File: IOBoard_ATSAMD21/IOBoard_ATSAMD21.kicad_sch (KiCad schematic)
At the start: 36 parts, among them J1 Conn_PIC_ICSP_ICD, J2 Conn_01x04_Male, SW1 EG_1218, SW2 EG_1218, SW3 EG_1218, SW4 EG_1218, U1 ATSAMD21G18A-A, U2 AP2112K-3.3

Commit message: IOBoard V2 + documentation
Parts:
- ENC0, ENC1, ENC2, ENC3: footprint Rotary_Encoder:RotaryEncoder_Bourns_Vertical_PEC12R-3xxxF-Sxxxx -> custom_lib:PEC12R-3217F-S0024-ND
- H1, H2, H3, H4: footprint MountingHole:MountingHole_2.2mm_M2_Pad -> MountingHole:MountingHole_3.2mm_M3_ISO7380_Pad
- SW1, SW2, SW3, SW4: footprint Custom:EG_1218 -> custom_lib:EG_1218
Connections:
- net GND: now also R1.1, R2.1, R3.1, R4.1; no longer D1.1 (K), D2.1 (K), D3.1 (K), D4.1 (K)
- net LED0: now also D1.2 (A); no longer R1.2
- net LED1: now also D2.2 (A); no longer R2.2
- net LED2: now also D3.2 (A); no longer R3.2
- net LED3: now also D4.2 (A); no longer R4.2
- net SCL: now also J2.3 (Pin_3); no longer J2.4 (Pin_4)
- net SDA: now also J2.4 (Pin_4); no longer J2.3 (Pin_3)
- new net: D2.1 (K), R2.2
- new net: D1.1 (K), R1.2
- new net: D4.1 (K), R4.2
- new net: D3.1 (K), R3.2
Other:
- moved on the sheet: R1, R2, R3, R4

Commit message: cleaned up'
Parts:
- added S? (x3): EG1218, digikey-footprints:Switch_Slide_11.6x4mm_EG1218, symbol dk_Slide-Switches:EG1218
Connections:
- new net Line In 1: S?.3
- new net Line In 2: S?.1
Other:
- note added: "CV config"
- note added: "Line Config"
- note added: "Line/CV SW"
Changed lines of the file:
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@@
+    (stroke (width 0) (type default) (color 0 0 0 0))
+  )
+  (polyline (pts (xy 181.61 127) (xy 181.61 158.75))
     (stroke (width 0) (type default) (color 0 0 0 0))
   )
@@
     (stroke (width 0) (type default) (color 0 0 0 0))
   )
+  (polyline (pts (xy 148.59 158.75) (xy 181.61 158.75))
+    (stroke (width 0) (type default) (color 0 0 0 0))
+  )
   (wire (pts (xy 234.95 53.34) (xy 240.03 53.34))
     (stroke (width 0) (type default) (color 0 0 0 0))
@@
   (polyline (pts (xy 148.59 196.85) (xy 148.59 179.07))
     (stroke (width 0) (type default) (color 0 0 0 0))
+  )
+  (text "Line/CV SW" (at 259.715 112.395 0)
+    (effects (font (size 1.27 1.27)) (justify left bottom))
+  )
+  (text "CV config" (at 233.045 126.365 0)
+    (effects (font (size 1.27 1.27)) (justify left bottom))
   )
   (text "LEDs" (at 91.44 196.85 0)
     (effects (font (size 2.5 2.5)) (justify left bottom))
   )
+  (text "Line Config" (at 152.4 130.81 0)
+    (effects (font (size 1.27 1.27)) (justify left bottom))
+  )
   (text "Debug Header\n" (at 121.92 48.26 0)
     (effects (font (size 2.5 2.5)) (justify left bottom))
@@
     (effects (font (size 1.27 1.27)) (justify right bottom))
   )
+  (label "Line In 1" (at 158.75 135.255 180)
+    (effects (font (size 1.27 1.27)) (justify right bottom))
+  )
   (label "ENC2_A" (at 38.1 95.25 180)
     (effects (font (size 1.27 1.27)) (justify right bottom))
@@
   )
   (label "VDDIO0" (at 222.25 34.29 180)
+    (effects (font (size 1.27 1.27)) (justify right bottom))
+  )
+  (label "Line In 2" (at 158.75 140.335 180)
     (effects (font (size 1.27 1.27)) (justify right bottom))
   )
@@
     (pin "1")
   )
+  (symbol (lib_id "dk_Slide-Switches:EG1218") (at 163.83 137.795 180) (unit 1)
+    (in_bom yes) (on_board yes) (fields_autoplaced)
+    (property "Reference" "S?" (id 0) (at 163.6268 130.175 0))
+    (property "Value" "EG1218" (id 1) (at 163.6268 132.715 0))
+    (property "Footprint" "digikey-footprints:Switch_Slide_11.6x4mm_EG1218" (id 2) (at 158.75 142.875 0)
+      (effects (font (size 1.27 1.27)) (justify left) hide)
+    )
+    (property "Datasheet" "http://spec_sheets.e-switch.com/specs/P040040.pdf" (id 3) (at 158.75 145.415 0)
+      (effects (font (size 1.524 1.524)) (justify left) hide)
+    )
+    (property "Digi-Key_PN" "EG1903-ND" (id 4) (at 158.75 147.955 0)
+      (effects (font (size 1.524 1.524)) (justify left) hide)
+    )
+    (property "MPN" "EG1218" (id 5) (at 158.75 150.495 0)
+      (effects (font (size 1.524 1.524)) (justify left) hide)
+    )
+    (property "Category" "Switches" (id 6) (at 158.75 153.035 0)
+      (effects (font (size 1.524 1.524)) (justify left) hide)
+    )
+    (property "Family" "Slide Switches" (id 7) (at 158.75 155.575 0)
+      (effects (font (size 1.524 1.524)) (justify left) hide)
+    )
+    (property "DK_Datasheet_Link" "http://spec_sheets.e-switch.com/specs/P040040.pdf" (id 8) (at 158.75 158.115 0)
+      (effects (font (size 1.524 1.524)) (justify left) hide)
+    )
+    (property "DK_Detail_Page" "/product-detail/en/e-switch/EG1218/EG1903-ND/101726" (id 9) (at 158.75 160.655 0)
+      (effects (font (size 1.524 1.524)) (justify left) hide)
+    )
+    (property "Description" "SWITCH SLIDE SPDT 200MA 30V" (id 10) (at 158.75 163.195 0)
+      (effects (font (size 1.524 1.524)) (justify left) hide)
+    )
+    (property "Manufacturer" "E-Switch" (id 11) (at 158.75 165.735 0)
+      (effects (font (size 1.524 1.524)) (justify left) hide)
+    )
+    (property "Status" "Active" (id 12) (at 158.75 168.275 0)
+      (effects (font (size 1.524 1.524)) (justify left) hide)
+    )
+    (pin "1")
+    (pin "2")
+    (pin "3")
+  )
   (symbol (lib_id "Device:C_Small") (at 29.21 30.48 0) (unit 1)
     (in_bom yes) (on_board yes) (fields_autoplaced)
@@
     (pin "4")
   )
+  (symbol (lib_id "dk_Slide-Switches:EG1218") (at 265.43 122.555 180) (unit 1)
+    (in_bom yes) (on_board yes) (fields_autoplaced)
+    (property "Reference" "S?" (id 0) (at 265.2268 114.3 0))
+    (property "Value" "EG1218" (id 1) (at 265.2268 116.84 0))
+    (property "Footprint" "digikey-footprints:Switch_Slide_11.6x4mm_EG1218" (id 2) (at 260.35 127.635 0)
+      (effects (font (size 1.27 1.27)) (justify left) hide)
+    )
+    (property "Datasheet" "http://spec_sheets.e-switch.com/specs/P040040.pdf" (id 3) (at 260.35 130.175 0)
+      (effects (font (size 1.524 1.524)) (justify left) hide)
+    )
+    (property "Digi-Key_PN" "EG1903-ND" (id 4) (at 260.35 132.715 0)
+      (effects (font (size 1.524 1.524)) (justify left) hide)
+    )
+    (property "MPN" "EG1218" (id 5) (at 260.35 135.255 0)
+      (effects (font (size 1.524 1.524)) (justify left) hide)
+    )
+    (property "Category" "Switches" (id 6) (at 260.35 137.795 0)
+      (effects (font (size 1.524 1.524)) (justify left) hide)
+    )
+    (property "Family" "Slide Switches" (id 7) (at 260.35 140.335 0)
+      (effects (font (size 1.524 1.524)) (justify left) hide)
+    )
+    (property "DK_Datasheet_Link" "http://spec_sheets.e-switch.com/specs/P040040.pdf" (id 8) (at 260.35 142.875 0)
+      (effects (font (size 1.524 1.524)) (justify left) hide)
+    )
+    (property "DK_Detail_Page" "/product-detail/en/e-switch/EG1218/EG1903-ND/101726" (id 9) (at 260.35 145.415 0)
+      (effects (font (size 1.524 1.524)) (justify left) hide)
+    )
+    (property "Description" "SWITCH SLIDE SPDT 200MA 30V" (id 10) (at 260.35 147.955 0)
+      (effects (font (size 1.524 1.524)) (justify left) hide)
+    )
+    (property "Manufacturer" "E-Switch" (id 11) (at 260.35 150.495 0)
+      (effects (font (size 1.524 1.524)) (justify left) hide)
+    )
+    (property "Status" "Active" (id 12) (at 260.35 153.035 0)
+      (effects (font (size 1.524 1.524)) (justify left) hide)
+    )
+    (pin "1")
+    (pin "2")
+    (pin "3")
+  )
   (symbol (lib_id "Device:C_Small") (at 262.89 63.5 270) (unit 1)
     (in_bom yes) (on_board yes) (fields_autoplaced)
@@
     )
     (pin "1")
+  )
+  (symbol (lib_id "dk_Slide-Switches:EG1218") (at 238.125 134.62 180) (unit 1)
+    (in_bom yes) (on_board yes) (fields_autoplaced)
+    (property "Reference" "S?" (id 0) (at 237.9218 127 0))
+    (property "Value" "EG1218" (id 1) (at 237.9218 129.54 0))
+    (property "Footprint" "digikey-footprints:Switch_Slide_11.6x4mm_EG1218" (id 2) (at 233.045 139.7 0)
+      (effects (font (size 1.27 1.27)) (justify left) hide)
+    )
+    (property "Datasheet" "http://spec_sheets.e-switch.com/specs/P040040.pdf" (id 3) (at 233.045 142.24 0)
+      (effects (font (size 1.524 1.524)) (justify left) hide)
+    )
+    (property "Digi-Key_PN" "EG1903-ND" (id 4) (at 233.045 144.78 0)
+      (effects (font (size 1.524 1.524)) (justify left) hide)
+    )
+    (property "MPN" "EG1218" (id 5) (at 233.045 147.32 0)
+      (effects (font (size 1.524 1.524)) (justify left) hide)
+    )
+    (property "Category" "Switches" (id 6) (at 233.045 149.86 0)
+      (effects (font (size 1.524 1.524)) (justify left) hide)
+    )
+    (property "Family" "Slide Switches" (id 7) (at 233.045 152.4 0)
+      (effects (font (size 1.524 1.524)) (justify left) hide)
+    )
+    (property "DK_Datasheet_Link" "http://spec_sheets.e-switch.com/specs/P040040.pdf" (id 8) (at 233.045 154.94 0)
+      (effects (font (size 1.524 1.524)) (justify left) hide)
+    )
+    (property "DK_Detail_Page" "/product-detail/en/e-switch/EG1218/EG1903-ND/101726" (id 9) (at 233.045 157.48 0)
+      (effects (font (size 1.524 1.524)) (justify left) hide)
+    )
+    (property "Description" "SWITCH SLIDE SPDT 200MA 30V" (id 10) (at 233.045 160.02 0)
+      (effects (font (size 1.524 1.524)) (justify left) hide)
+    )
+    (property "Manufacturer" "E-Switch" (id 11) (at 233.045 162.56 0)
+      (effects (font (size 1.524 1.524)) (justify left) hide)
+    )
+    (property "Status" "Active" (id 12) (at 233.045 165.1 0)
+      (effects (font (size 1.524 1.524)) (justify left) hide)
+    )
+    (pin "1")
+    (pin "2")
+    (pin "3")
   )
   (symbol (lib_id "power:PWR_FLAG") (at 166.37 187.96 0) (unit 1)
@@
       (reference "R5") (unit 1) (value "10k") (footprint "Resistor_SMD:R_0603_1608Metric")
     )
+    (path "/159198b4-3db9-4754-9af5-96c41cca56cd"
+      (reference "S?") (unit 1) (value "EG1218") (footprint "digikey-footprints:Switch_Slide_11.6x4mm_EG1218")
+    )
+    (path "/1de66764-f42d-4311-af86-085dcb5b98c8"
+      (reference "S?") (unit 1) (value "EG1218") (footprint "digikey-footprints:Switch_Slide_11.6x4mm_EG1218")
+    )
+    (path "/30d0b158-2f75-41a0-a330-f1db3d645a68"
+      (reference "S?") (unit 1) (value "EG1218") (footprint "digikey-footprints:Switch_Slide_11.6x4mm_EG1218")
+    )
     (path "/db87f46b-2fb8-44ca-a6d9-59159164f5d8"

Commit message: jack
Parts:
- added J13: Eurorack_Mono_Jack, winterbloom:AudioJack_WQP518MA, symbol winterbloom:Eurorack_Mono_Jack
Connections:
- new net GNDA: J13.S (Sleeve)
- new net IN4: J13.T (Tip)
- no-connect marks 0 -> 1
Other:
- note added: "TN: NC T: Tip (signal) S: GND"
- note added: "TN: a switch connected to the input. Could be used to change between jack inputs and CV inputs. NC for now."

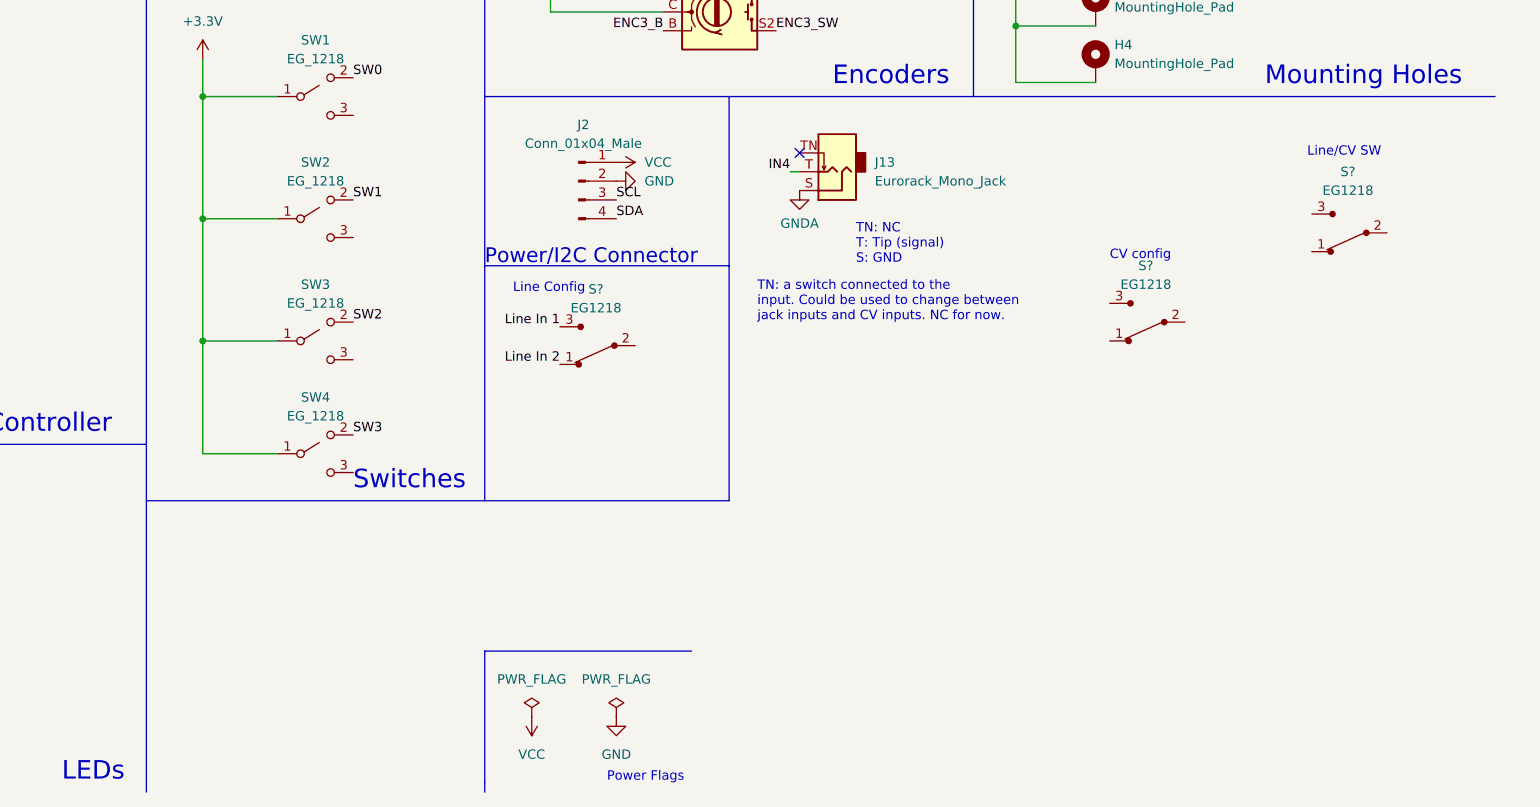
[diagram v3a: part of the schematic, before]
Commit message: added firmware
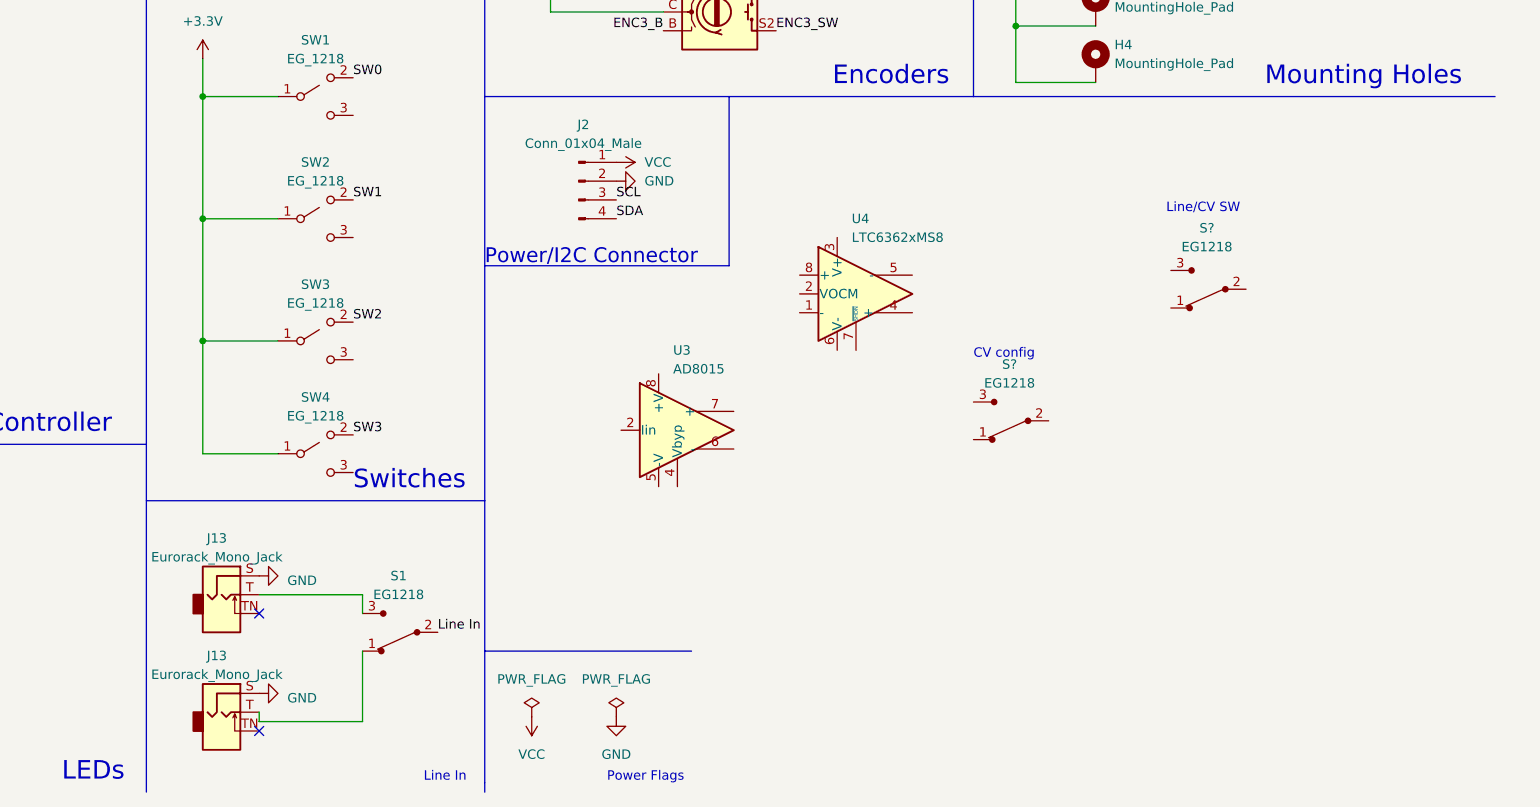
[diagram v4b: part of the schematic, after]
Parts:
- removed S?: EG1218, digikey-footprints:Switch_Slide_11.6x4mm_EG1218, symbol dk_Slide-Switches:EG1218
- added J13: Eurorack_Mono_Jack, winterbloom:AudioJack_WQP518MA, symbol winterbloom:Eurorack_Mono_Jack
- added S1: EG1218, digikey-footprints:Switch_Slide_11.6x4mm_EG1218, symbol dk_Slide-Switches:EG1218
- added U3: AD8015, Package_SO:SOIC-8_3.9x4.9mm_P1.27mm, symbol Amplifier_Operational:AD8015
- added U4: LTC6362xMS8, Package_SO:MSOP-8_3x3mm_P0.65mm, symbol Amplifier_Operational:LTC6362xMS8
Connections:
- net GNDA is gone; now on net GND: J13.S (Sleeve)
- net GND: now also J13.S (Sleeve)
- net IN4: no longer names the net of J13.T (Tip)
- net IN4: now also S1.3
- new net: J13.T (Tip), S1.1
- new net Line In: S1.2
- no-connect marks 1 -> 2
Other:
- note added: "Line In"
- note removed: "Line Config"
- note removed: "TN: NC T: Tip (signal) S: GND"
- note removed: "TN: a switch connected to the input. Could be used to change between jack inputs and CV inputs. NC for now."
- moved on the sheet: J13, S?
